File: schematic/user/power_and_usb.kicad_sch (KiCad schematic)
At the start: 25 parts, among them IC1 FS312F-G, J1 TYPE-C-31-M-04, Q1 FS8205, Q2 AO3401A, U1 TP4056, U2 MAX17048G+T10, U3 TLV1117-33

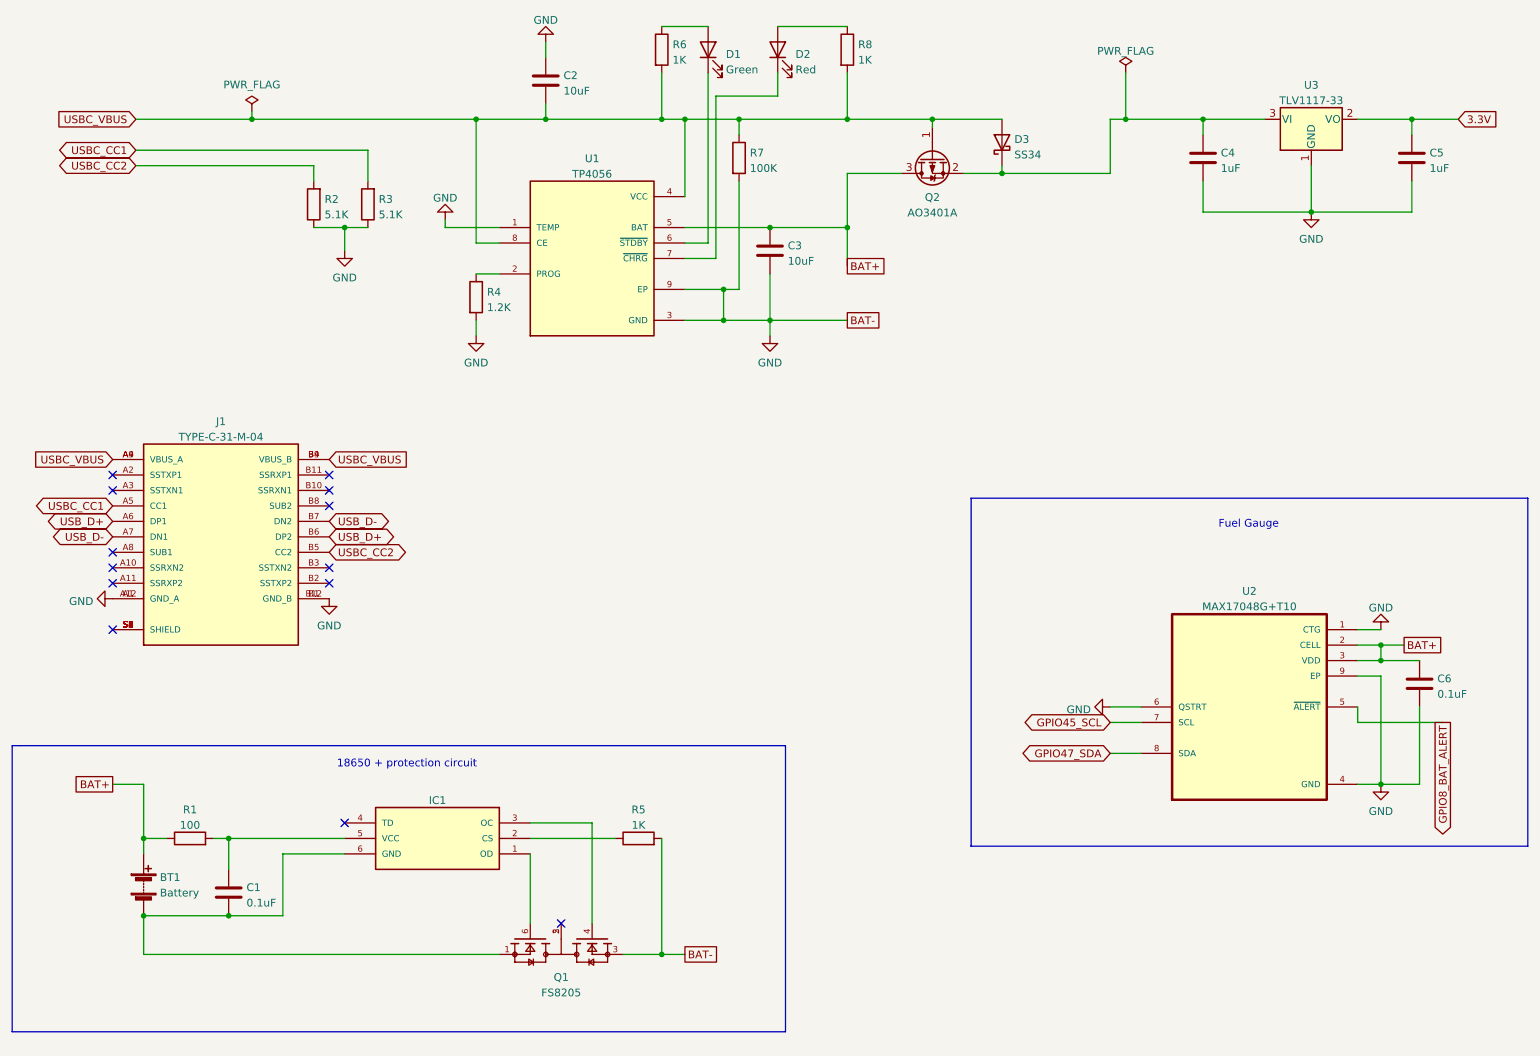
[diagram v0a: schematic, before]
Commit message: v0.4 board: add MOSFET power control for TLV320 and other peripherals
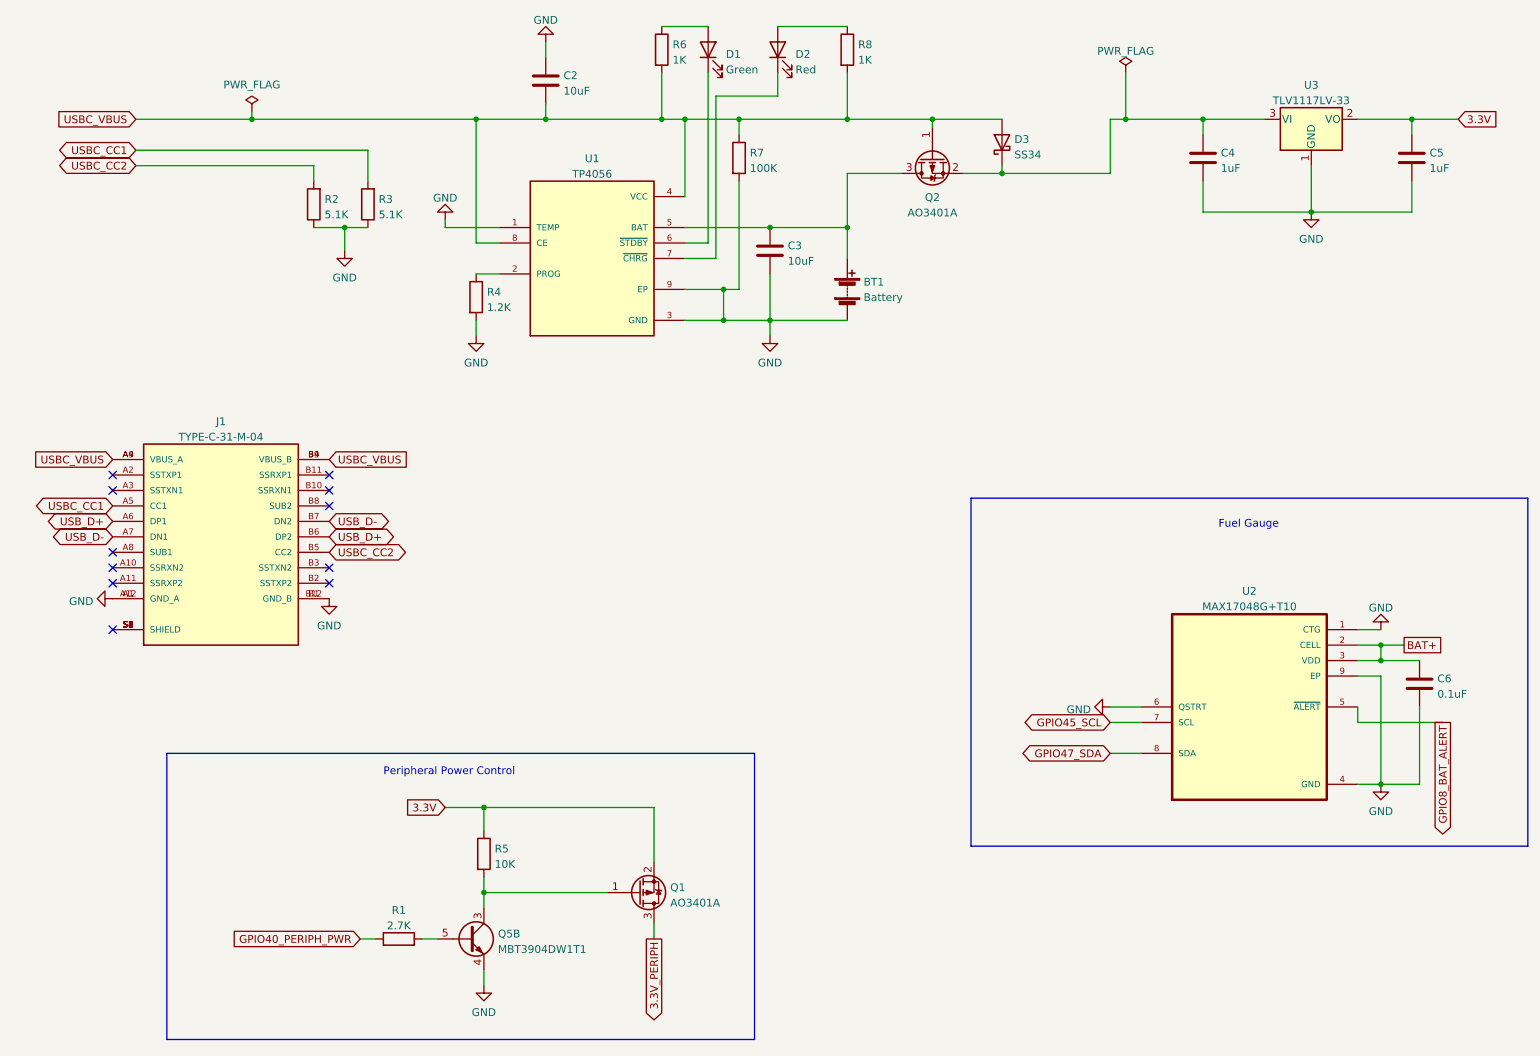
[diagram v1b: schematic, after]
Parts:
- removed C1: 0.1uF, Capacitor_SMD:C_0402_1005Metric, symbol Device:C
- removed IC1: FS312F-G, ezDV_production:SOT23-6, symbol FS312F-G:FS312F-G
- removed Q1: FS8205, ezDV_production:SOT95P280X145-6N, symbol FS8205:FS8205
- added Q1: AO3401A, Package_TO_SOT_SMD:SOT-23, symbol Transistor_FET:AO3401A
- added Q5: MBT3904DW1T1, Package_TO_SOT_SMD:SOT-363_SC-70-6, symbol Transistor_BJT:MBT2222ADW1T1
- R1: value 100 -> 2.7K; footprint Resistor_SMD:R_0402_1005Metric -> Resistor_SMD:R_0603_1608Metric; LCSC C25076 -> C269437
- R5: value 1K -> 10K; LCSC C85373 -> C25744
- U3: value TLV1117-33 -> TLV1117LV-33
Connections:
- net 3.3V: now also R5.1, Q1.2 (S)
- net BAT+: no longer BT1.1 (+), C3.1, Q2.3 (D), R1.1, U1.5 (BAT)
- net GND: now also BT1.2 (-), Q5.4 (E2); no longer R5.2
- net at R1.2: now also Q5.5 (B2)
- new net: BT1.1 (+), C3.1, Q2.3 (D), U1.5 (BAT)
- new net: Q1.1 (G), Q5.3 (C2), R5.2
- new net 3.3V_PERIPH: Q1.3 (D)
- new net GPIO40_PERIPH_PWR: R1.1
- no-connect marks 13 -> 11
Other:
- note added: "Peripheral Power Control"
- note removed: "18650 + protection circuit"
- moved on the sheet: BT1

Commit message: v0.4 board: substitute JLCPCB basic parts where possible ($3/component savings).
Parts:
- Q5: LCSC (none) -> C110150
- R1: LCSC C269437 -> C13167
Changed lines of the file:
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@@
       (effects (font (size 1.27 1.27)) hide)
     )
-    (property "Datasheet" "https://datasheet.lcsc.com/lcsc/1811101310_TyoHM-RMC06032-7K5-N_C269437.pdf" (id 3) (at 92.71 170.18 0)
-      (effects (font (size 1.27 1.27)) hide)
-    )
-    (property "LCSC" "C269437" (id 4) (at 92.71 170.18 0)
+    (property "Datasheet" "https://datasheet.lcsc.com/lcsc/2206010216_UNI-ROYAL-Uniroyal-Elec-0603WAF2701T5E_C13167.pdf" (id 3) (at 92.71 170.18 0)
+      (effects (font (size 1.27 1.27)) hide)
+    )
+    (property "LCSC" "C13167" (id 4) (at 92.71 170.18 0)
       (effects (font (size 1.27 1.27)) hide)
     )
@@
       (effects (font (size 1.27 1.27)) hide)
     )
-    (property "Datasheet" "http://www.onsemi.com/pub_link/Collateral/MBT2222ADW1T1-D.PDF" (id 3) (at 104.14 170.18 0)
-      (effects (font (size 1.27 1.27)) hide)
-    )
+    (property "Datasheet" "https://datasheet.lcsc.com/lcsc/1811151434_onsemi-MBT3904DW1T1G_C110150.pdf" (id 3) (at 104.14 170.18 0)
+      (effects (font (size 1.27 1.27)) hide)
+    )
+    (property "LCSC" "C110150" (id 4) (at 104.14 170.18 0)
+      (effects (font (size 1.27 1.27)) hide)
+    )

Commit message: v0.4 board: increase power trace width, reposition decoupling caps, add missing depop resistors
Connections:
- net BAT+: now also BT1.1 (+), C3.1, Q2.3 (D), U1.5 (BAT)
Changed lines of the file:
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@@
+    (stroke (width 0) (type default) (color 0 0 0 0))
+  )
+  (wire (pts (xy 166.37 53.34) (xy 168.91 53.34))
     (stroke (width 0) (type default) (color 0 0 0 0))
   )
@@
       (effects (font (size 1.27 1.27)) (justify left) hide)
     )
+  )
+  (global_label "BAT+" (shape passive) (at 168.91 53.34 0) (fields_autoplaced)
+    (effects (font (size 1.27 1.27)) (justify left))
+    (property "Intersheet References" "${INTERSHEET_REFS}" (id 0) (at 176.2217 53.2606 0)
+      (effects (font (size 1.27 1.27)) (justify left) hide)
+    )

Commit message: v0.4 board: add thermistors for battery safety
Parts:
- added R25: 80.6K, Resistor_SMD:R_0603_1608Metric, symbol Device:R
- added R27: 4.87K, Resistor_SMD:R_0805_2012Metric, symbol Device:R
- added TH1: SDNT2012X103F3950FTF, Resistor_SMD:R_0805_2012Metric, symbol Device:Thermistor_NTC
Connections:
- net GND: now also R25.2, TH1.1; no longer U1.1 (TEMP)
- net USBC_VBUS: now also R27.1
- new net TP4056_NTC: R25.1, R27.2, TH1.2, U1.1 (TEMP)
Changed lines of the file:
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@@
   (junction (at 212.09 35.56) (diameter 0) (color 0 0 0 0)
   )
+  (junction (at 166.37 68.58) (diameter 0) (color 0 0 0 0)
+  )
   (junction (at 83.82 53.34) (diameter 0) (color 0 0 0 0)
   )
@@
   (junction (at 106.68 148.59) (diameter 0) (color 0 0 0 0)
   )
+  (junction (at 99.06 35.56) (diameter 0) (color 0 0 0 0)
+  )
   (junction (at 254 144.78) (diameter 0) (color 0 0 0 0)
   )
@@
   )
   (junction (at 146.05 63.5) (diameter 0) (color 0 0 0 0)
+  )
+  (junction (at 99.06 53.34) (diameter 0) (color 0 0 0 0)
+  )
+  (junction (at 105.41 69.85) (diameter 0) (color 0 0 0 0)
   )
   (no_connect (at 45.72 96.52))
@@
     (stroke (width 0) (type default) (color 0 0 0 0))
   )
+  (wire (pts (xy 105.41 69.85) (xy 105.41 71.12))
+    (stroke (width 0) (type default) (color 0 0 0 0))
+  )
   (wire (pts (xy 83.82 53.34) (xy 87.63 53.34))
     (stroke (width 0) (type default) (color 0 0 0 0))
@@
     (stroke (width 0) (type default) (color 0 0 0 0))
   )
-  (wire (pts (xy 100.33 52.07) (xy 100.33 53.34))
+  (wire (pts (xy 99.06 69.85) (xy 105.41 69.85))
     (stroke (width 0) (type default) (color 0 0 0 0))
   )
@@
     (stroke (width 0) (type default) (color 0 0 0 0))
   )
+  (wire (pts (xy 99.06 53.34) (xy 92.71 53.34))
+    (stroke (width 0) (type default) (color 0 0 0 0))
+  )
   (wire (pts (xy 264.16 134.62) (xy 250.19 134.62))
     (stroke (width 0) (type default) (color 0 0 0 0))
@@
     (stroke (width 0) (type default) (color 0 0 0 0))
   )
+  (wire (pts (xy 163.83 82.55) (xy 166.37 82.55))
+    (stroke (width 0) (type default) (color 0 0 0 0))
+  )
   (wire (pts (xy 106.68 160.02) (xy 106.68 162.56))
     (stroke (width 0) (type default) (color 0 0 0 0))
   )
+  (wire (pts (xy 92.71 53.34) (xy 92.71 57.15))
+    (stroke (width 0) (type default) (color 0 0 0 0))
+  )
   (polyline (pts (xy 54.61 139.7) (xy 151.13 139.7))
     (stroke (width 0) (type default) (color 0 0 0 0))
@@
     (stroke (width 0) (type default) (color 0 0 0 0))
   )
+  (wire (pts (xy 99.06 53.34) (xy 109.22 53.34))
+    (stroke (width 0) (type default) (color 0 0 0 0))
+  )
+  (wire (pts (xy 99.06 53.34) (xy 96.52 58.42))
+    (stroke (width 0) (type default) (color 0 0 0 0))
+  )
   (wire (pts (xy 105.41 35.56) (xy 116.84 35.56))
     (stroke (width 0) (type default) (color 0 0 0 0))
@@
     (stroke (width 0) (type default) (color 0 0 0 0))
   )
-  (wire (pts (xy 105.41 68.58) (xy 105.41 71.12))
+  (wire (pts (xy 105.41 68.58) (xy 105.41 69.85))
+    (stroke (width 0) (type default) (color 0 0 0 0))
+  )
+  (wire (pts (xy 96.52 66.04) (xy 99.06 69.85))
     (stroke (width 0) (type default) (color 0 0 0 0))
   )
@@
     (stroke (width 0) (type default) (color 0 0 0 0))
   )
-  (wire (pts (xy 100.33 53.34) (xy 109.22 53.34))
-    (stroke (width 0) (type default) (color 0 0 0 0))
-  )
   (wire (pts (xy 144.78 58.42) (xy 139.7 58.42))
     (stroke (width 0) (type default) (color 0 0 0 0))
@@
     (stroke (width 0) (type default) (color 0 0 0 0))
   )
+  (wire (pts (xy 166.37 82.55) (xy 166.37 80.01))
+    (stroke (width 0) (type default) (color 0 0 0 0))
+  )
+  (wire (pts (xy 99.06 46.99) (xy 99.06 53.34))
+    (stroke (width 0) (type default) (color 0 0 0 0))
+  )
   (wire (pts (xy 166.37 27.94) (xy 166.37 35.56))
     (stroke (width 0) (type default) (color 0 0 0 0))
@@
     (stroke (width 0) (type default) (color 0 0 0 0))
   )
-  (wire (pts (xy 68.58 35.56) (xy 105.41 35.56))
+  (wire (pts (xy 166.37 68.58) (xy 166.37 72.39))
+    (stroke (width 0) (type default) (color 0 0 0 0))
+  )
+  (wire (pts (xy 68.58 35.56) (xy 99.06 35.56))
     (stroke (width 0) (type default) (color 0 0 0 0))
   )
@@
   )
   (wire (pts (xy 139.7 68.58) (xy 146.05 68.58))
+    (stroke (width 0) (type default) (color 0 0 0 0))
+  )
+  (wire (pts (xy 99.06 35.56) (xy 99.06 39.37))
+    (stroke (width 0) (type default) (color 0 0 0 0))
+  )
+  (wire (pts (xy 99.06 35.56) (xy 105.41 35.56))
     (stroke (width 0) (type default) (color 0 0 0 0))
   )
@@
     )
   )
+  (global_label "TP4056_NTC" (shape output) (at 163.83 82.55 180) (fields_autoplaced)
+    (effects (font (size 1.27 1.27)) (justify right))
+    (property "Intersheet References" "${INTERSHEET_REFS}" (id 0) (at 149.8055 82.4706 0)
+      (effects (font (size 1.27 1.27)) (justify right) hide)
+    )
+  )
   (global_label "GPIO40_PERIPH_PWR" (shape input) (at 86.36 170.18 180) (fields_autoplaced)
     (effects (font (size 1.27 1.27)) (justify right))
@@
     (effects (font (size 1.27 1.27)) (justify right))
     (property "Intersheet References" "${INTERSHEET_REFS}" (id 0) (at 37.3198 40.5606 0)
+      (effects (font (size 1.27 1.27)) (justify right) hide)
+    )
+  )
+  (global_label "TP4056_NTC" (shape input) (at 92.71 57.15 270) (fields_autoplaced)
+    (effects (font (size 1.27 1.27)) (justify right))
+    (property "Intersheet References" "${INTERSHEET_REFS}" (id 0) (at 92.6306 71.1745 90)
       (effects (font (size 1.27 1.27)) (justify right) hide)
     )
@@
     )
     (property "Datasheet" "~" (id 3) (at 212.09 27.94 0)
-      (effects (font (size 1.27 1.27)) hide)
-    )
-    (pin "1")
-  )
-  (symbol (lib_id "power:GND") (at 100.33 52.07 180) (unit 1)
-    (in_bom yes) (on_board yes) (fields_autoplaced)
-    (property "Reference" "#PWR04" (id 0) (at 100.33 45.72 0)
-      (effects (font (size 1.27 1.27)) hide)
-    )
-    (property "Value" "GND" (id 1) (at 100.33 48.4942 0))
-    (property "Footprint" "" (id 2) (at 100.33 52.07 0)
-      (effects (font (size 1.27 1.27)) hide)
-    )
-    (property "Datasheet" "" (id 3) (at 100.33 52.07 0)
       (effects (font (size 1.27 1.27)) hide)
     )
@@
     (pin "S8")
   )
+  (symbol (lib_id "Device:Thermistor_NTC") (at 166.37 76.2 0) (unit 1)
+    (in_bom yes) (on_board yes) (fields_autoplaced)
+    (property "Reference" "TH1" (id 0) (at 168.783 75.6828 0)
+      (effects (font (size 1.27 1.27)) (justify left))
+    )
+    (property "Value" "SDNT2012X103F3950FTF" (id 1) (at 168.783 78.2197 0)
+      (effects (font (size 1.27 1.27)) (justify left))
+    )
+    (property "Footprint" "Resistor_SMD:R_0805_2012Metric" (id 2) (at 166.37 74.93 0)
+      (effects (font (size 1.27 1.27)) hide)
+    )
+    (property "Datasheet" "https://datasheet.lcsc.com/lcsc/2110081230_Sunlord-SDNT2012X103F3950FTF_C95968.pdf" (id 3) (at 166.37 74.93 0)
+      (effects (font (size 1.27 1.27)) hide)
+    )
+    (property "LCSC" "C95968" (id 4) (at 166.37 76.2 0)
+      (effects (font (size 1.27 1.27)) hide)
+    )
+    (pin "1")
+    (pin "2")
+  )
   (symbol (lib_id "Device:R") (at 105.41 64.77 0) (unit 1)
     (in_bom yes) (on_board yes) (fields_autoplaced)
@@
       (effects (font (size 1.27 1.27)) hide)
     )
+    (pin "1")
+    (pin "2")
+  )
+  (symbol (lib_id "Device:R") (at 96.52 62.23 0) (unit 1)
+    (in_bom yes) (on_board yes) (fields_autoplaced)
+    (property "Reference" "R25" (id 0) (at 98.298 61.3953 0)
+      (effects (font (size 1.27 1.27)) (justify left))
+    )
+    (property "Value" "80.6K" (id 1) (at 98.298 63.9322 0)
+      (effects (font (size 1.27 1.27)) (justify left))
+    )
+    (property "Footprint" "Resistor_SMD:R_0603_1608Metric" (id 2) (at 94.742 62.23 90)
+      (effects (font (size 1.27 1.27)) hide)
+    )
+    (property "Datasheet" "https://datasheet.lcsc.com/lcsc/1912111437_PANASONIC-ERJ3EKF8062V_C403361.pdf" (id 3) (at 96.52 62.23 0)
+      (effects (font (size 1.27 1.27)) hide)
+    )
+    (property "LCSC" "C403361" (id 4) (at 96.52 62.23 0)
+      (effects (font (size 1.27 1.27)) hide)
+    )
+    (pin "1")
+    (pin "2")
+  )
+  (symbol (lib_id "Device:R") (at 99.06 43.18 0) (unit 1)
+    (in_bom yes) (on_board yes) (fields_autoplaced)
+    (property "Reference" "R27" (id 0) (at 100.838 42.3453 0)
+      (effects (font (size 1.27 1.27)) (justify left))
+    )
+    (property "Value" "4.87K" (id 1) (at 100.838 44.8822 0)
+      (effects (font (size 1.27 1.27)) (justify left))
+    )
+    (property "Footprint" "Resistor_SMD:R_0805_2012Metric" (id 2) (at 97.282 43.18 90)
+      (effects (font (size 1.27 1.27)) hide)
+    )
+    (property "Datasheet" "https://datasheet.lcsc.com/lcsc/1810261826_Viking-Tech-ARG05FTC4871_C218605.pdf" (id 3) (at 99.06 43.18 0)
+      (effects (font (size 1.27 1.27)) hide)
+    )
+    (property "LCSC" "C218605" (id 4) (at 99.06 43.18 0)
+      (effects (font (size 1.27 1.27)) hide)
+    )

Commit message: v0.4 board submitted for build/assembly.
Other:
- company: (none) -> FreeDV Project
- title: (none) -> ezDV Power and USB
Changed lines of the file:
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@@
 (kicad_sch (version 20211123) (generator eeschema)
   (paper "A4")
+  (title_block
+    (title "ezDV Power and USB")
+    (date "2022-10-01")
+    (rev "v0.4")
+    (company "FreeDV Project")
+  )
   (junction (at 224.79 35.56) (diameter 0) (color 0 0 0 0)
   )

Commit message: v0.5 board: move PERIPH_PWR GPIO to RTC to make sure it stays off when sleeping.
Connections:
- net GPIO40_PERIPH_PWR renamed GPIO17_PERIPH_PWR
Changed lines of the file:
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@@
     )
   )
-  (global_label "GPIO40_PERIPH_PWR" (shape input) (at 86.36 170.18 180) (fields_autoplaced)
+  (global_label "GPIO17_PERIPH_PWR" (shape input) (at 86.36 170.18 180) (fields_autoplaced)
     (effects (font (size 1.27 1.27)) (justify right))
     (property "Intersheet References" "${INTERSHEET_REFS}" (id 0) (at 64.2317 170.1006 0)

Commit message: v0.5 board: move SCL to GPIO 48 as 45 is a ESP32 strapping pin.
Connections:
- net GPIO45_SCL renamed GPIO48_SCL
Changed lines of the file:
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@@
     )
   )
-  (global_label "GPIO45_SCL" (shape bidirectional) (at 209.55 134.62 180) (fields_autoplaced)
+  (global_label "GPIO48_SCL" (shape bidirectional) (at 209.55 134.62 180) (fields_autoplaced)
     (effects (font (size 1.27 1.27)) (justify right))
     (property "Intersheet References" "${INTERSHEET_REFS}" (id 0) (at 195.7674 134.5406 0)
